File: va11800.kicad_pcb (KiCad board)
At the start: 2 copper layers, 389.5 x 166.4 mm, 256 parts, among them J1 Conn_01x16_Female, J2 Conn_01x16_Female, J6 D2, j1 MX-NoLED, k1 MX-NoLED, m1 MX-NoLED, p1 MX-NoLED, q1 MX-NoLED, t1 MX-NoLED, u1 MX-NoLED, x1 MX-NoLED, y1 MX-NoLED

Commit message: corrected switch placement
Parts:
- moved capslock1 1.68 mm to (37.3, 174.8)
- moved left1 1.62 mm to (287.7, 218.3)
- moved up1 1.51 mm to (306.8, 199.3)
- moved down1 1.50 mm to (306.8, 218.3)
- moved right1 1.35 mm to (325.8, 218.3)
- moved R_mod1 1.12 mm to (208.2, 212.9)
- moved R_mod3 1.12 mm to (253.4, 212.9)
- moved space1 1.12 mm to (143.9, 212.9)
- moved R_mod2_alt1 1.12 mm to (232.0, 212.9)
- moved R_mod2 1.12 mm to (224.8, 212.9)
- moved space3 1.12 mm to (136.7, 212.9)
- moved lm1 1.12 mm to (34.3, 212.9)
- moved lm2 1.12 mm to (62.9, 212.9)
- moved R_mod3_alt1 1.12 mm to (251.0, 212.9)
- moved NUBS1 1.12 mm to (53.4, 193.9)
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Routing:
- net row10: track 762.0 -> 710.2 mm
- net row11: track 785.1 -> 736.1 mm
- net row9: track 663.2 -> 614.4 mm
- net row12: track 775.1 -> 728.3 mm
- net row7: track 723.8 -> 684.9 mm
- net col6: track 546.5 -> 507.9 mm
- net row6: track 728.9 -> 690.4 mm
- net row5: track 664.7 -> 626.8 mm
- net row8: track 707.8 -> 670.6 mm
- net row4: track 697.5 -> 660.4 mm
- net row13: track 839.9 -> 810.5 mm
- net col0: track 916.3 -> 936.9 mm
- net col7: track 592.8 -> 577.6 mm
- net col4: track 551.0 -> 554.2 mm
- net col8: track 569.9 -> 572.2 mm
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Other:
- board size 389.5 x 166.4 mm -> 390.2 x 166.5 mm
- net class Default removed

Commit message: remove front and back silkscreen and front mask from switch pads
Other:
- board size 390.2 x 166.5 mm -> 391.2 x 166.5 mm

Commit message: reconect disconnected tracks
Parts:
- renumbered D76 to D1, D95 to D10, D108 to D100, D15 to D101, D36 to D102, D56 to D103, D72 to D104, D54 to D105, D30 to D106, D34 to D107, D55 to D108, D16 to D109, D122 to D11, D35 to D110, D91 to D111, D33 to D112, D32 to D113, D53 to D114, D18 to D12, D2 to D13, D39 to D14, D60 to D15, D78 to D16, D96 to D17, D3 to D18, D94 to D2, D40 to D20, D61 to D21, D79 to D22, D97 to D23, D75 to D25, D20 to D26, D4 to D27, D41 to D28, D62 to D29, D121 to D3, D80 to D30, D98 to D31, D5 to D32, D21 to D33, D42 to D34, D63 to D35, D81 to D36, D99 to D37, D6 to D38, D43 to D39, D1 to D4, D64 to D40, D82 to D41, D100 to D42, D120 to D43, D22 to D44, D7 to D45, D23 to D46, D44 to D47, D65 to D48, D83 to D49, D37 to D5, D101 to D50, D114 to D51, D45 to D52, D66 to D53, D84 to D54, D102 to D55, D8 to D56, D24 to D57, D46 to D58, D67 to D59, D58 to D6, D85 to D60, D103 to D61, D115 to D62, D9 to D63, D25 to D64, D47 to D65, D68 to D66, D86 to D67, D104 to D68, D117 to D69, D38 to D7, D10 to D70, D26 to D71, D48 to D72, D69 to D73, D87 to D74, D105 to D75, D118 to D76, D49 to D77, D70 to D78, D88 to D79, D59 to D8, D57 to D80, D11 to D81, D27 to D82, D12 to D83, D71 to D84, D17 to D85, D31 to D86, D107 to D87, D74 to D88, D124 to D89, D77 to D9, D50 to D90, D51 to D91, D52 to D92, D13 to D93, D28 to D94, D92 to D95, D116 to D96, D29 to D97, D73 to D98, D14 to D99, J2 to J3, L_mod3 to L_mod1, R1 to R2, R2 to R3, R3 to R4, d1 to d24, f5 to f10, f6 to f12, f12 to f13, f7 to f2, f2 to f3, f8 to f4, f3 to f5, f9 to f6, f13 to f7, f4 to f8, f10 to f9, h1 to h6, j1 to j2, kp_+3 to kp_+2, kp_+2 to kp_+3, kp_7 to kp_1, kp_8 to kp_2, kp_6 to kp_3, kp_3 to kp_4, kp_1 to kp_5, kp_4 to kp_6, kp_9 to kp_7, kp_2 to kp_8, kp_5 to kp_9, kp_enter3 to kp_enter1, kp_enter1 to kp_enter2, kp_enter2 to kp_enter3, kp_zero2 to kp_zero1, kp_zero1 to kp_zero2, left_shift2 to left_shift1, left_shift1 to left_shift2, n9 to n10, n0 to n11, n10 to n8, n8 to n9
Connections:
- D43 pad 2: Net-(D120-Pad2) -> Net-(space1-Pad2)
- J1 pad 1: Net-(J1-Pad1) -> unconnected-(J1-Pad1)
- J1 pad 2: Net-(J1-Pad2) -> unconnected-(J1-Pad2)
- J3 pad 14: Net-(J2-Pad14) -> unconnected-(J3-Pad14)
- J3 pad 15: Net-(J2-Pad15) -> unconnected-(J3-Pad15)
- J3 pad 16: Net-(J2-Pad16) -> unconnected-(J3-Pad16)
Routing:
- net row10: track 710.2 -> 757.5 mm
- net row9: track 614.4 -> 661.7 mm
- net row12: track 728.3 -> 775.5 mm
- net row11: track 736.1 -> 783.2 mm
- net col6: track 507.9 -> 546.0 mm
- net row7: track 684.9 -> 722.3 mm
- net row6: track 690.4 -> 727.4 mm
- net row5: track 626.8 -> 663.3 mm
- net row4: track 660.4 -> 696.3 mm
- net row8: track 670.6 -> 706.2 mm
- net row13: track 810.5 -> 841.7 mm
- net Net-(space1-Pad2): track 14.1 -> 25.0 mm
- net Net-(D120-Pad2): track 10.0 -> 0.00 mm
- net Net-(D96-Pad2): track 7.76 -> 5.98 mm
- net Net-(D62-Pad2): track 7.63 -> 5.98 mm
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
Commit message: correct traces and mounting holes
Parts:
- D1, D10, D100, D101, D102, D103, D104, D105, D106, D107, D108, D109, D11, D110, D111, D112, D113, D114, D12, D13, D14, D15, D16, D17, D18, D19, D2, D20, D21, D22, D23, D25, D26, D27, D28, D29, D3, D30, D31, D32, D33, D34, D35, D36, D37, D38, D39, D4, D40, D41, D42, D43, D44, D45, D46, D47, D48, D49, D5, D50, D51, D52, D53, D54, D55, D56, D57, D58, D59, D6, D60, D61, D62, D63, D64, D65, D66, D67, D68, D69, D7, D70, D71, D72, D73, D74, D75, D76, D77, D78, D79, D8, D80, D81, D82, D83, D84, D86, D87, D88, D89, D9, D91, D93, D94, D95, D96, D97, D98, D99: footprint vuckale:Diode -> keebio:Diode-dual
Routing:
- net col5: track 434.5 -> 457.4 mm
- net row12: track 775.5 -> 797.5 mm
- net col3: track 598.0 -> 614.5 mm
- net row8: track 706.2 -> 722.3 mm
- net row6: track 727.4 -> 741.9 mm
- net row10: track 757.5 -> 771.1 mm
- net col0: track 936.9 -> 923.7 mm
- net col1: track 790.5 -> 803.4 mm
- net col7: track 577.3 -> 587.0 mm
- net row2: track 378.4 -> 387.6 mm
- net row0: track 502.7 -> 510.6 mm
- net col2: track 648.0 -> 655.5 mm
- net col4: track 552.9 -> 559.6 mm
- net row1: track 448.9 -> 454.2 mm
- net row3: track 384.0 -> 389.3 mm
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
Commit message: fix encoder placement and add 6u spacebar support
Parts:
- added D115: D_Small, keebio:Diode-dual, B.Cu at (189.8, 212.9)
- added R5: R_Small, keebio:Resistor-Hybrid, B.Cu at (265.6, 97.5)
- added R6: R_Small, keebio:Resistor-Hybrid, B.Cu at (263.7, 80.9)
- added ResetSwitch1: RESET, Button_Switch_SMD:SW_SPST_TL3342, F.Cu at (173.2, 212.6)
- added ResetSwitch2: RESET, Button_Switch_SMD:SW_SPST_TL3342, F.Cu at (238.3, 89.3)
- added RmodX1: MX-NoLED, MX_Only:MXOnly-1U-NoLED, F.Cu at (201.0, 212.9)
- added SW1: RotaryEncoder_Switch, keebio:RotaryEncoder_EC11, F.Cu at (392.3, 79.1)
- added SW2: RotaryEncoder_Switch, keebio:RotaryEncoder_EC11, F.Cu at (276.2, 79.8)
- added SW3: RotaryEncoder_Switch, keebio:RotaryEncoder_EC11, F.Cu at (296.3, 136.7)
- added SW4: RotaryEncoder_Switch, keebio:RotaryEncoder_EC11, F.Cu at (29.6, 136.7)
- added SW5: RotaryEncoder_Switch, keebio:RotaryEncoder_EC11, F.Cu at (392.3, 155.3)
- added space4: MX-NoLED, MX_Only:MXOnly-6U-NoSwitch, F.Cu at (134.3, 212.9)
- moved J6 3.94 mm to (395.4, 164.9)
- moved D69 3.26 mm to (192.5, 213.0)
- moved D86 2.28 mm to (309.9, 138.7)
- moved D91 2.25 mm to (307.0, 138.7)
- moved R2 1.38 mm to (297.4, 78.6)
- moved R3 1.27 mm to (307.4, 78.7)
- moved R4 1.14 mm to (317.6, 78.8)
- moved D5 0.99 mm to (39.1, 138.6)
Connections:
- net Net-(D80-Pad2) renamed en-row11
- net Net-(D91-Pad2) renamed en3-row5
- J1 pad 2: unconnected-(J1-Pad2) -> RST
- J3 pad 14: unconnected-(J3-Pad14) -> A
- J3 pad 15: unconnected-(J3-Pad15) -> B
- J3 pad 16: unconnected-(J3-Pad16) -> B2
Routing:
- net A: track 0.00 -> 711.8 mm, vias 0 -> 9
- net GND: track 512.4 -> 1190.7 mm, vias 4 -> 16
- net RST: track 0.00 -> 603.7 mm, vias 0 -> 5
- net B2R1: track 0.00 -> 360.5 mm, vias 0 -> 3
- net B: track 0.00 -> 259.7 mm, vias 0 -> 1
- net B2: track 0.00 -> 108.5 mm, vias 0 -> 3
- net col6: track 544.2 -> 623.8 mm
- net row4: track 698.4 -> 720.7 mm
- net row0: track 510.6 -> 532.0 mm
- net en3-row5: track 9.37 -> 27.7 mm, vias 0 -> 1
- net Net-(D109-Pad2): track 8.51 -> 25.1 mm
- net Net-(D69-Pad2): track 28.2 -> 43.3 mm
- net col0: track 923.7 -> 938.8 mm
- net Net-(RmodX1-Pad2): track 0.00 -> 14.3 mm
- net Net-(D5-Pad2): track 7.46 -> 15.0 mm
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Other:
- board text added: "(A,D/B/E)"
- board text added: "0Ω"
- board text added: "10/2022"
- board text added: "6.25u(B)"
- board text added: "6.25u(C)"
- board text added: "6u(E)"
- board text added: "7u/6.25u(A,D/C)"
- board text added: "7u/6.25u/6u"
- board text added: "RESET"
- board text removed: "02/2022"

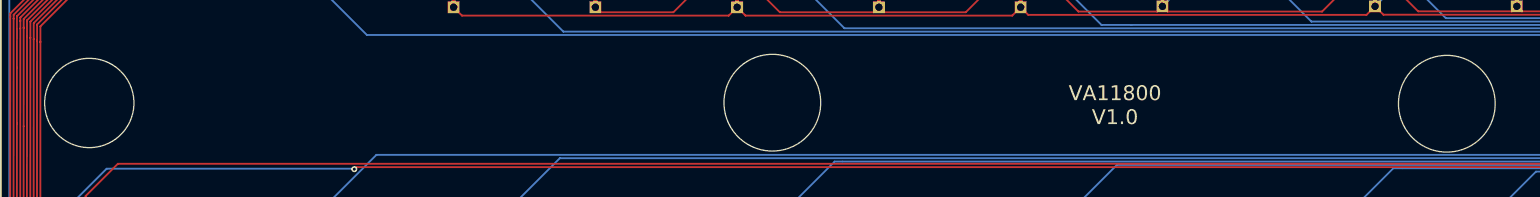
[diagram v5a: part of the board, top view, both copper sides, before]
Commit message: fix pads on switch footprint
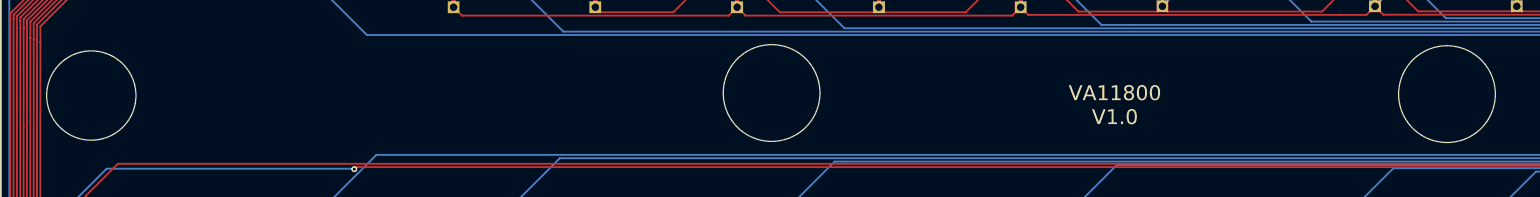
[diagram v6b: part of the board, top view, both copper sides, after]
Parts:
- moved H5 1.30 mm to (118.9, 116.0)
- moved H3 1.29 mm to (209.7, 116.2)
- moved H1 1.04 mm to (27.5, 116.4)
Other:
- board text added: "X/2022"
- board text removed: "10/2022"

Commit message: cleanup traces
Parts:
- added ?: , , F.Cu at (257.5, 63.7)
- moved R6 40.4 mm to (267.9, 121.1), turned to 0 degrees
- moved R5 26.3 mm to (267.9, 123.7), turned to 180 degrees
- moved J6 7.54 mm to (403.0, 164.9)
- moved D86 2.97 mm to (307.0, 137.9)
- moved D91 2.94 mm to (309.9, 137.9)
- moved J6 1.58 mm to (257.5, 63.7)
- moved D101 1.48 mm to (382.0, 82.1)
- moved D80 0.22 mm to (382.0, 154.9)
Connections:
- J3 pad 14: A -> B2
- J3 pad 15: B -> A
- J3 pad 16: B2 -> B
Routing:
- net GND: track 1190.7 -> 1337.4 mm, vias 16 -> 1
- net col6: track 623.8 -> 712.2 mm
- net row10: track 771.1 -> 843.4 mm
- net col8: track 574.3 -> 512.8 mm
- net B2R1: track 360.5 -> 417.2 mm, vias 3 -> 0
- net B2R2: track 6.18 -> 57.7 mm
- net Net-(D88-Pad2): track 32.2 -> 82.6 mm
- net A: track 711.8 -> 756.1 mm, vias 9 -> 0
- net row8: track 722.3 -> 765.1 mm
- net row6: track 741.9 -> 781.5 mm
- net row4: track 720.7 -> 760.2 mm
- net B2: track 108.5 -> 73.3 mm, vias 3 -> 0
- net row12: track 794.2 -> 827.8 mm
- net row2: track 387.6 -> 413.9 mm
- net Net-(D11-Pad2): track 48.9 -> 74.0 mm
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
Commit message: fix ground for encoder and reset switch and trace cleanup
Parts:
- moved ResetSwitch1 2.30 mm to (171.0, 213.0)
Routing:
- net GND: track 1337.4 -> 1665.6 mm, vias 1 -> 3
- net col4: track 562.9 -> 682.5 mm
- net row6: track 781.5 -> 820.5 mm
- net row4: track 760.2 -> 790.7 mm
- net row5: track 676.6 -> 705.0 mm
- net col1: track 803.4 -> 829.5 mm, vias 1 -> 0
- net col2: track 655.5 -> 675.6 mm, vias 1 -> 0
- net col0: track 938.8 -> 955.6 mm, vias 1 -> 0
- net col8: track 512.8 -> 528.9 mm
- net RST: track 603.7 -> 589.7 mm, vias 5 -> 3
- net Net-(D4-Pad2): track 18.4 -> 29.4 mm
- net col7: track 589.1 -> 594.9 mm
- net B: track 246.8 -> 251.9 mm
- net col6: track 712.2 -> 707.5 mm
- net CapsLock: track 73.9 -> 70.7 mm
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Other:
- board text added: "GND"
- board text added: "RST"
